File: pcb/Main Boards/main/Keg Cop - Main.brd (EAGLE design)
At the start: 85 x 51 mm, 20 parts, among them IC1 DS18B20+

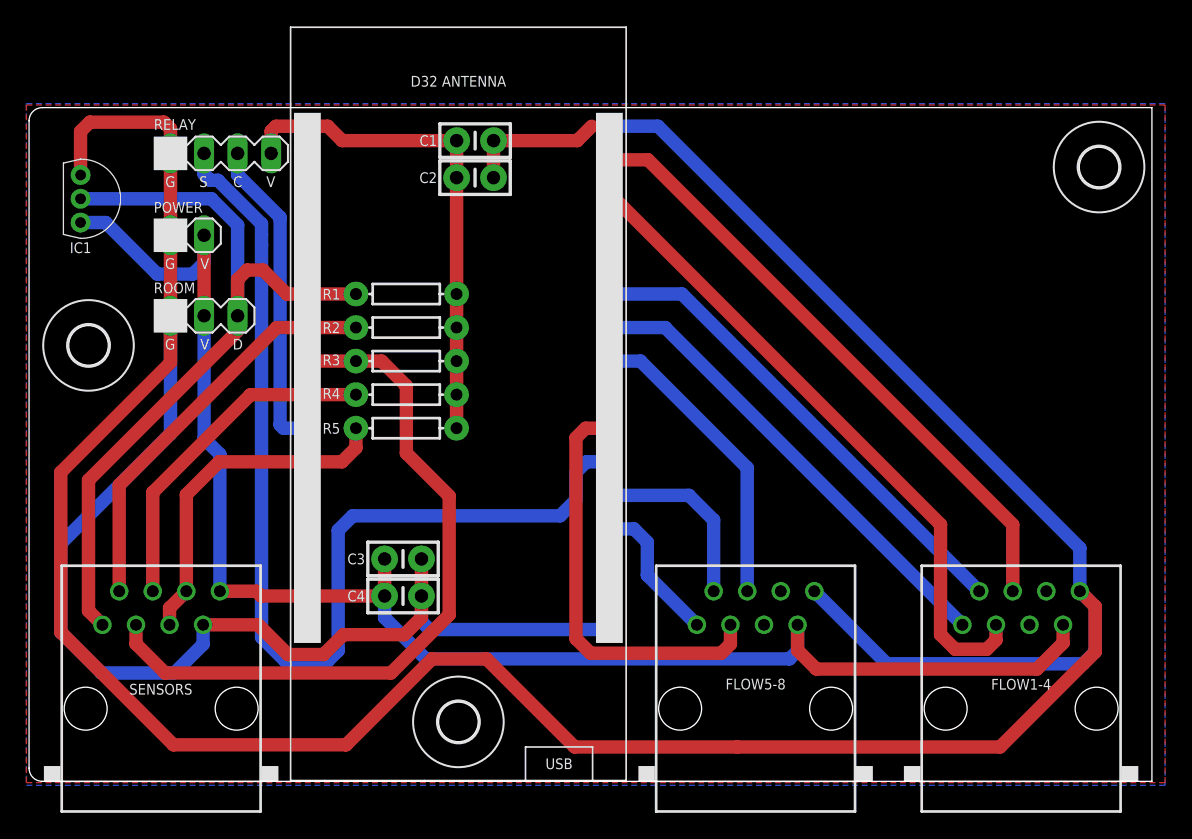
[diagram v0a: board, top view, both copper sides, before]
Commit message: Rewire, move to 9 meters
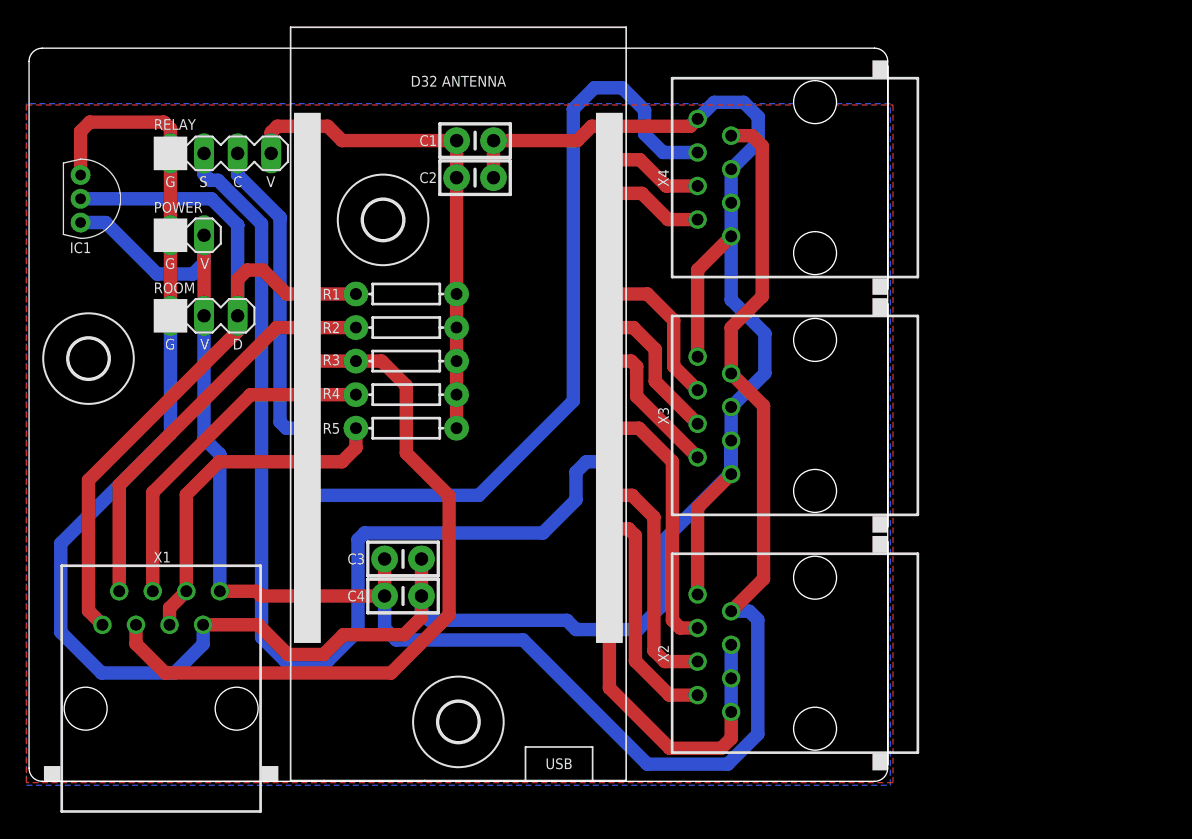
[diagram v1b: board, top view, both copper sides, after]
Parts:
- removed FLOW1-4, FLOW5-8: RJ45-8X, con-tycoelectronics:RJ45-NO-SHIELD
- added X2, X3, X4: RJ45-8X, con-tycoelectronics:RJ45-NO-SHIELD
- moved U$3 54.3 mm to (26.8, 42.5)
- moved U$1 1.00 mm to (4.50, 32.0)
- renumbered SENSORS to X1
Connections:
- new net KEG0: D32.IO0, X2.2
- net 5V: now also X2.7, X3.7, X4.7; no longer FLOW1-4.7, FLOW5-8.7
- net GND: now also X2.1, X2.3, X2.5, X2.8, X3.1, X3.3, X3.5, X3.8, X4.1, X4.3, X4.5, X4.8; no longer FLOW1-4.8, FLOW5-8.8
- net KEG1: now also D32.IO4, X2.4; no longer D32.IO0, FLOW5-8.1
- net KEG2: now also D32.IO17, X2.6; no longer D32.IO4, FLOW5-8.2
- net KEG3: now also D32.IO18, X3.2; no longer D32.IO17, FLOW5-8.3
- net KEG4: now also D32.IO19, X3.4; no longer D32.IO18, FLOW5-8.4
- net KEG5: now also D32.IO21, X3.6; no longer D32.IO19, FLOW1-4.1
- net KEG6: now also D32.IO22, X4.2; no longer D32.IO21, FLOW1-4.2
- net KEG7: now also D32.IO23, X4.4; no longer D32.IO22, FLOW1-4.3
- net KEG8: now also D32.IO12, X4.6; no longer D32.IO23, FLOW1-4.4
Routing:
- net GND: track 320.5 -> 222.8 mm
- net KEG7: track 49.9 -> 7.50 mm
- net KEG6: track 37.3 -> 7.50 mm
- net 5V: track 117.5 -> 144.0 mm
- net KEG5: track 36.0 -> 11.7 mm
- net KEG3: track 31.9 -> 11.0 mm
- net KEG0: track 0.00 -> 17.5 mm
- net KEG4: track 23.1 -> 11.1 mm
- net KEG8: track 47.0 -> 58.3 mm
- net KEG1: track 11.1 -> 17.8 mm
- net KEG2: track 14.1 -> 20.0 mm
- net SOL: track 78.7 -> 77.4 mm
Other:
- board size 85 x 51 mm -> 65 x 55.5 mm
- board text added: "1 - GND 2 - FL0 3 - GND 4 - FL1 5 - GND 6 - FL2 7 - 5VD 8 - GND"
- board text added: "1 - GND 2 - FL4 3 - GND 4 - FL5 5 - GND 6 - FL6 7 - 5VD 8 - GND"
- board text added: "1 - GND 2 - FL6 3 - GND 4 - FL7 5 - GND 6 - FL8 7 - 5VD 8 - GND"
- board text removed: "1 - FLOW1 2 - FLOW2 3 - FLOW3 4 - FLOW4"
- board text removed: "1 - FLOW5 2 - FLOW6 3 - FLOW7 4 - FLOW8"
- board text removed: "7 - 5V 8 - GND"

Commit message: Add pullups, move KEG0 to GPIO13
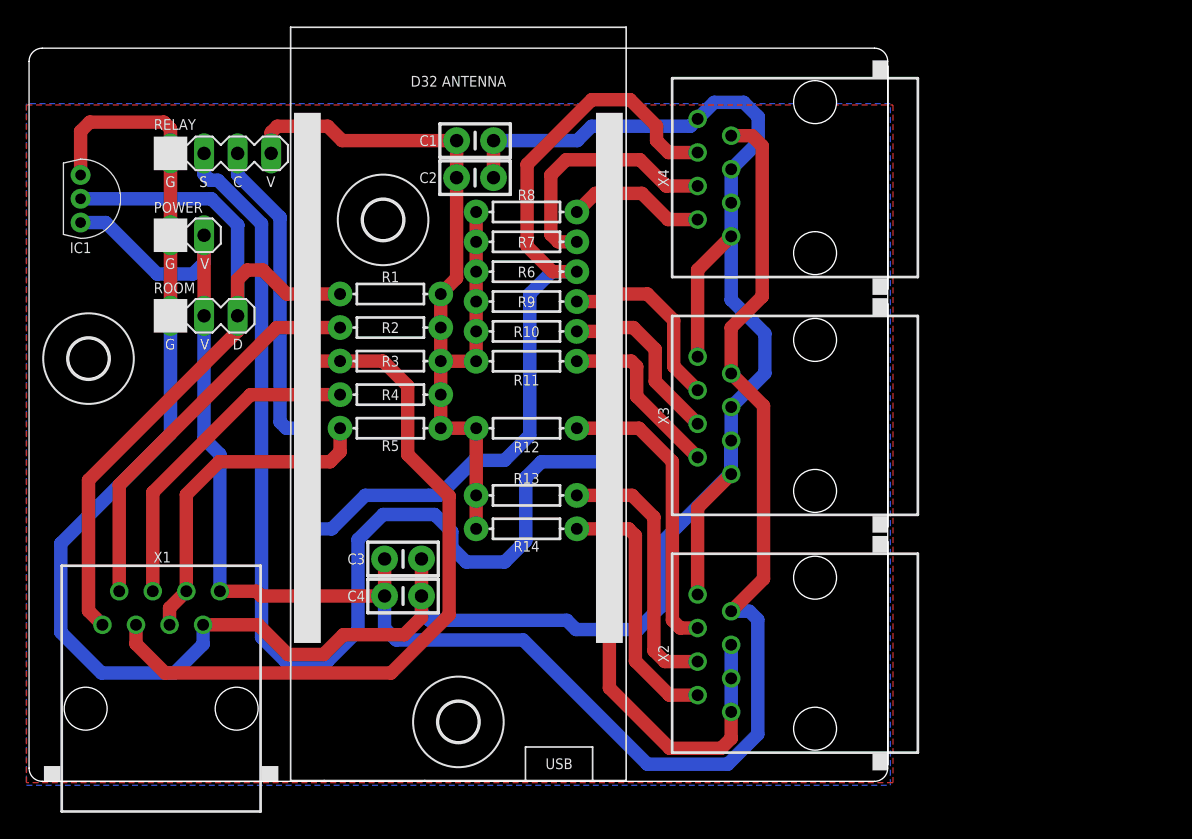
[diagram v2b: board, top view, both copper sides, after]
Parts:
- added R10, R11, R12, R13, R14, R6, R7, R8, R9: 2.2kΩ, SparkFun-Resistors:AXIAL-0.3
- moved R1 1.20 mm to (27.4, 36.9)
- moved R2 1.20 mm to (27.4, 34.3)
- moved R3 1.20 mm to (27.4, 31.8)
- moved R4 1.20 mm to (27.4, 29.3)
- moved R5 1.20 mm to (27.4, 26.7)
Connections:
- net 3V3: now also R10.P$2, R11.P$2, R12.P$2, R13.P$2, R14.P$2, R6.P$2, R7.P$2, R8.P$2, R9.P$2
- net KEG0: now also R14.P$1
- net KEG1: now also R13.P$1
- net KEG2: now also R12.P$1
- net KEG3: now also R11.P$1
- net KEG4: now also R10.P$1
- net KEG5: now also R9.P$1
- net KEG6: now also R8.P$1
- net KEG7: now also R7.P$1
- net KEG8: now also D32.IO13, R6.P$1; no longer D32.IO12
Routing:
- net 3V3: track 38.0 -> 62.8 mm
- net KEG7: track 7.50 -> 19.1 mm
- net SOL: track 77.4 -> 82.7 mm
- net KEG8: track 58.3 -> 62.7 mm
- net KEG6: track 7.50 -> 10.6 mm
- net KEG5: track 11.7 -> 14.4 mm
- net KEG4: track 11.1 -> 13.7 mm
- net KEG3: track 11.0 -> 13.5 mm
- net KEG1: track 17.8 -> 20.3 mm
- net KEG0: track 17.5 -> 19.9 mm
- net KEG2: track 20.0 -> 22.4 mm
- net TDAT: track 30.9 -> 29.7 mm
- net LDAT: track 26.1 -> 24.9 mm
- net RDAT: track 60.8 -> 59.6 mm
- net KDAT: track 26.2 -> 25.1 mm
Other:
- board text added: "1 - RDAT 2 - TDAT 3 - UDAT 4 - LDAT 5 - KDAT 6 - DNC 7 - GND 8 - 5V"
- board text added: "Keg Cop Main Board v 1.0 https://www.kegcop.com By @lbussy"
- board text removed: "1 - RDAT 2 - TDAT 3 - UDAT 4 - LDAT"
- board text removed: "5 - KDAT 6 - DNC 7 - GND 8 - 5V"
